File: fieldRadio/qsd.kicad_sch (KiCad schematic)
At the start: 41 parts, among them IC1 MCP1801, IC2 SN74LVC1G04DBVT, IC3 SN74AUP2G79DCUR, IC4 TS5A23157, IC5 SN74CBTLV3253, Q1 J309, T1 T50-TRIFILAR, U1 OPA1678

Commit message: Updating field radio
Continued schematic work on field radio
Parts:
- removed C18, C21: 1nF, Capacitor_SMD:C_0603_1608Metric_Pad1.08x0.95mm_HandSolder, symbol qsd_revB-eagle-import:CAP0603-CAP
- removed R18, R19, R26, R27: 100, Resistor_SMD:R_0603_1608Metric_Pad0.98x0.95mm_HandSolder, symbol qsd_revB-eagle-import:RESISTOR0603-RES
- removed R28: 7.5k, Resistor_SMD:R_0603_1608Metric_Pad0.98x0.95mm_HandSolder, symbol qsd_revB-eagle-import:RESISTOR0603-RES
- removed R31: 10k, Resistor_SMD:R_0603_1608Metric_Pad0.98x0.95mm_HandSolder, symbol qsd_revB-eagle-import:RESISTOR0603-RES
- removed R32: 5K, qsd_revB:RTRIM3296W, symbol qsd_revB-eagle-import:R-TRIMM3296W
- removed R9: R-TRIMM3296W, qsd_revB:RTRIM3296W, symbol qsd_revB-eagle-import:R-TRIMM3296W
- removed U1: OPA1678, Package_SO:SOIC-8_3.9x4.9mm_P1.27mm, symbol Amplifier_Operational:OPA1678
- added C8, C9: 0.1uF, Capacitor_SMD:C_0603_1608Metric_Pad1.08x0.95mm_HandSolder, symbol qsd_revB-eagle-import:CAP0603-CAP
- added IC6, IC7: INA821ID, SOIC127P600X175-8N, symbol SamacSys_Parts:INA821ID
- added R11, R12, R13, R4: 47k, Resistor_SMD:R_0603_1608Metric_Pad0.98x0.95mm_HandSolder, symbol qsd_revB-eagle-import:RESISTOR0603-RES
- added R2, R3: 49.9, Resistor_SMD:R_0603_1608Metric_Pad0.98x0.95mm_HandSolder, symbol qsd_revB-eagle-import:RESISTOR0603-RES
- added R9: 4.32K, Resistor_SMD:R_0603_1608Metric_Pad0.98x0.95mm_HandSolder, symbol qsd_revB-eagle-import:RESISTOR0603-RES
- C12, C14: value 0.22uF -> 0.1uF
- C13, C15: value 0.22uF -> 470pF
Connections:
- net 0-DEG: now also C13.2, IC6.4 (+IN), R4.2; no longer C12.2
- net 180-DEG: now also C13.1, IC6.1 (-IN), R11.2; no longer C13.2
- net 270-DEG: now also IC7.1 (-IN), R12.2
- net 90-DEG: now also C15.1, IC7.4 (+IN), R13.2; no longer C14.2
- net GND: now also C12.2, C8.1, C9.1, IC6.5 (-VS), IC7.5 (-VS), R11.1, R12.1, R13.1, R4.1, R9.1; no longer C12.1, C13.1, C15.1
- net Iout: now also IC6.7 (OUT)
- net Qout: now also IC7.7 (OUT)
- net at C6.2, C7.1 (+), R8.1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: now also R9.2
- net VCC5 renamed VDD5
- net VDD5: now also C8.2, C9.2, IC6.8 (+VS), IC7.8 (+VS)
- new net: IC7.2 (RG_1), R2.1
- new net: IC7.3 (RG_2), R2.2
- new net: IC6.2 (RG_1), R3.1
- new net: IC6.3 (RG_2), R3.2
- new net vbias: C12.1, C14.2, IC6.6 (REF), IC7.6 (REF)
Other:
- note added: "VBIAS"

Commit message: More schematic dev.
More schematic development
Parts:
- renumbered C1 to C128, C2 to C129, C3 to C130, C4 to C131, C16 to C132, C5 to C133, C6 to C134, C7 to C135, C10 to C136, C11 to C137, C13 to C138, C15 to C139, C8 to C140, C9 to C141, C12 to C142, C14 to C143, C19 to C144, C20 to C145, JP7 to JP3, Q1 to Q24, R1 to R143, R5 to R144, R6 to R145, R7 to R146, R8 to R147, R9 to R148, R10 to R149, R4 to R150, R11 to R151, R12 to R152, R13 to R153, R2 to R154, R3 to R155, T1 to T2

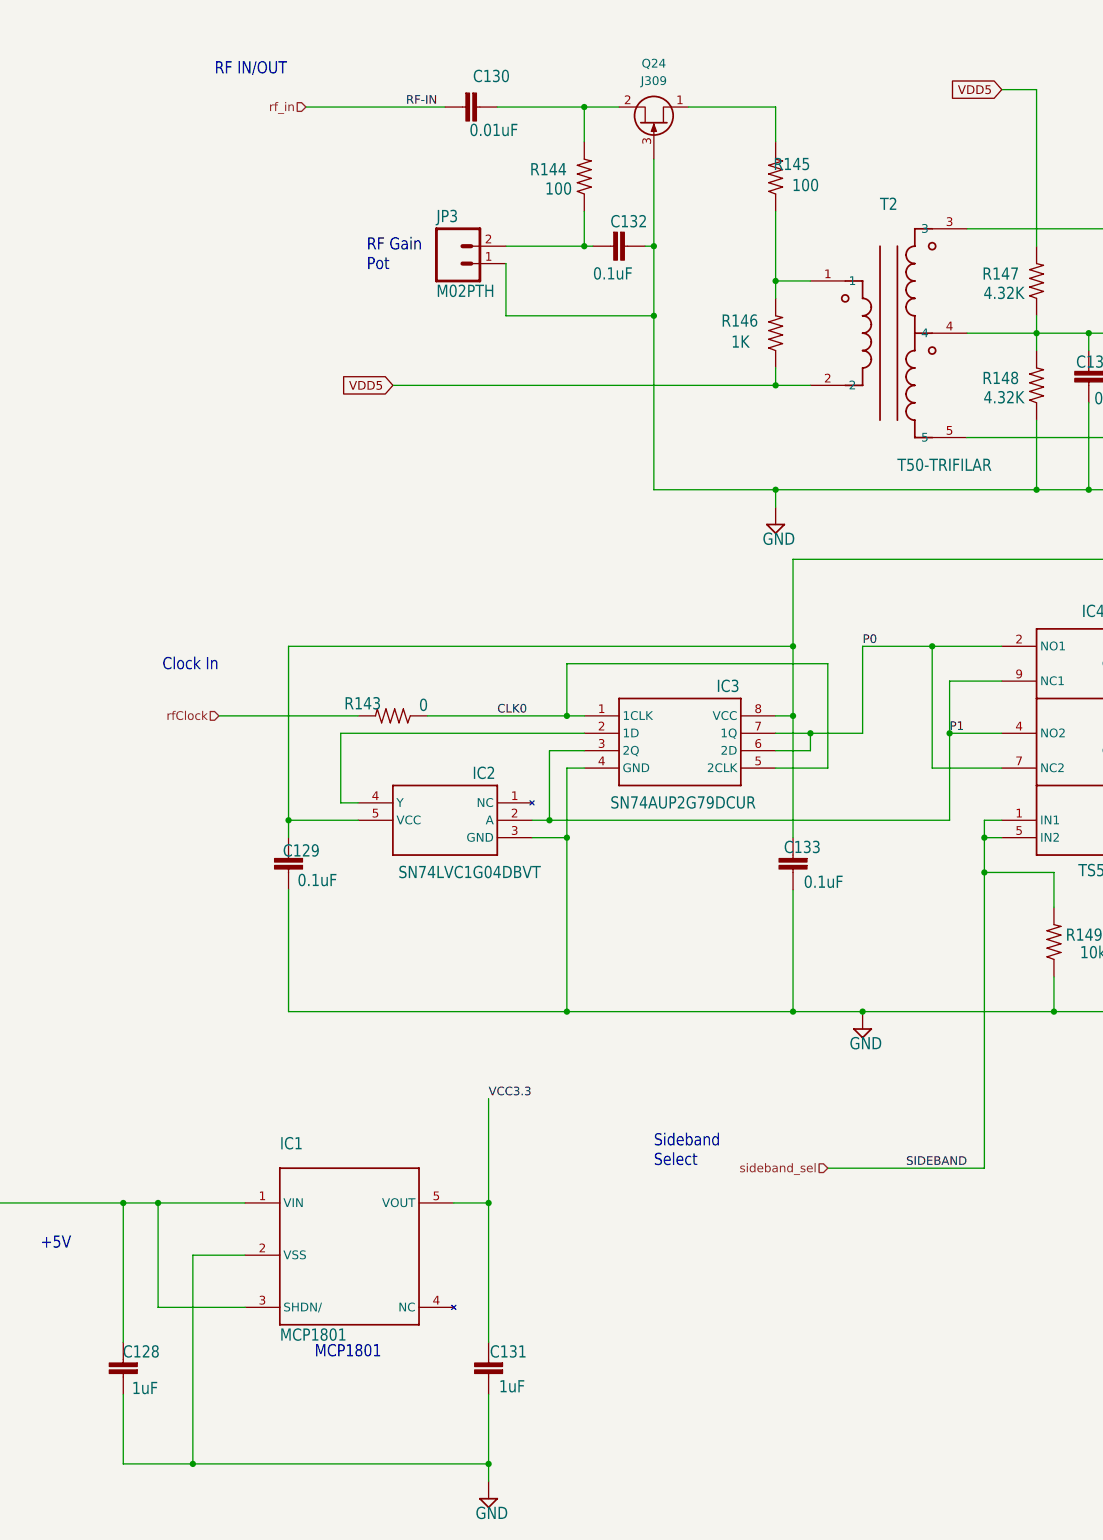
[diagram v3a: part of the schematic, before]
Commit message: Update Connectors
Changed to PCB mount connectors for back panel
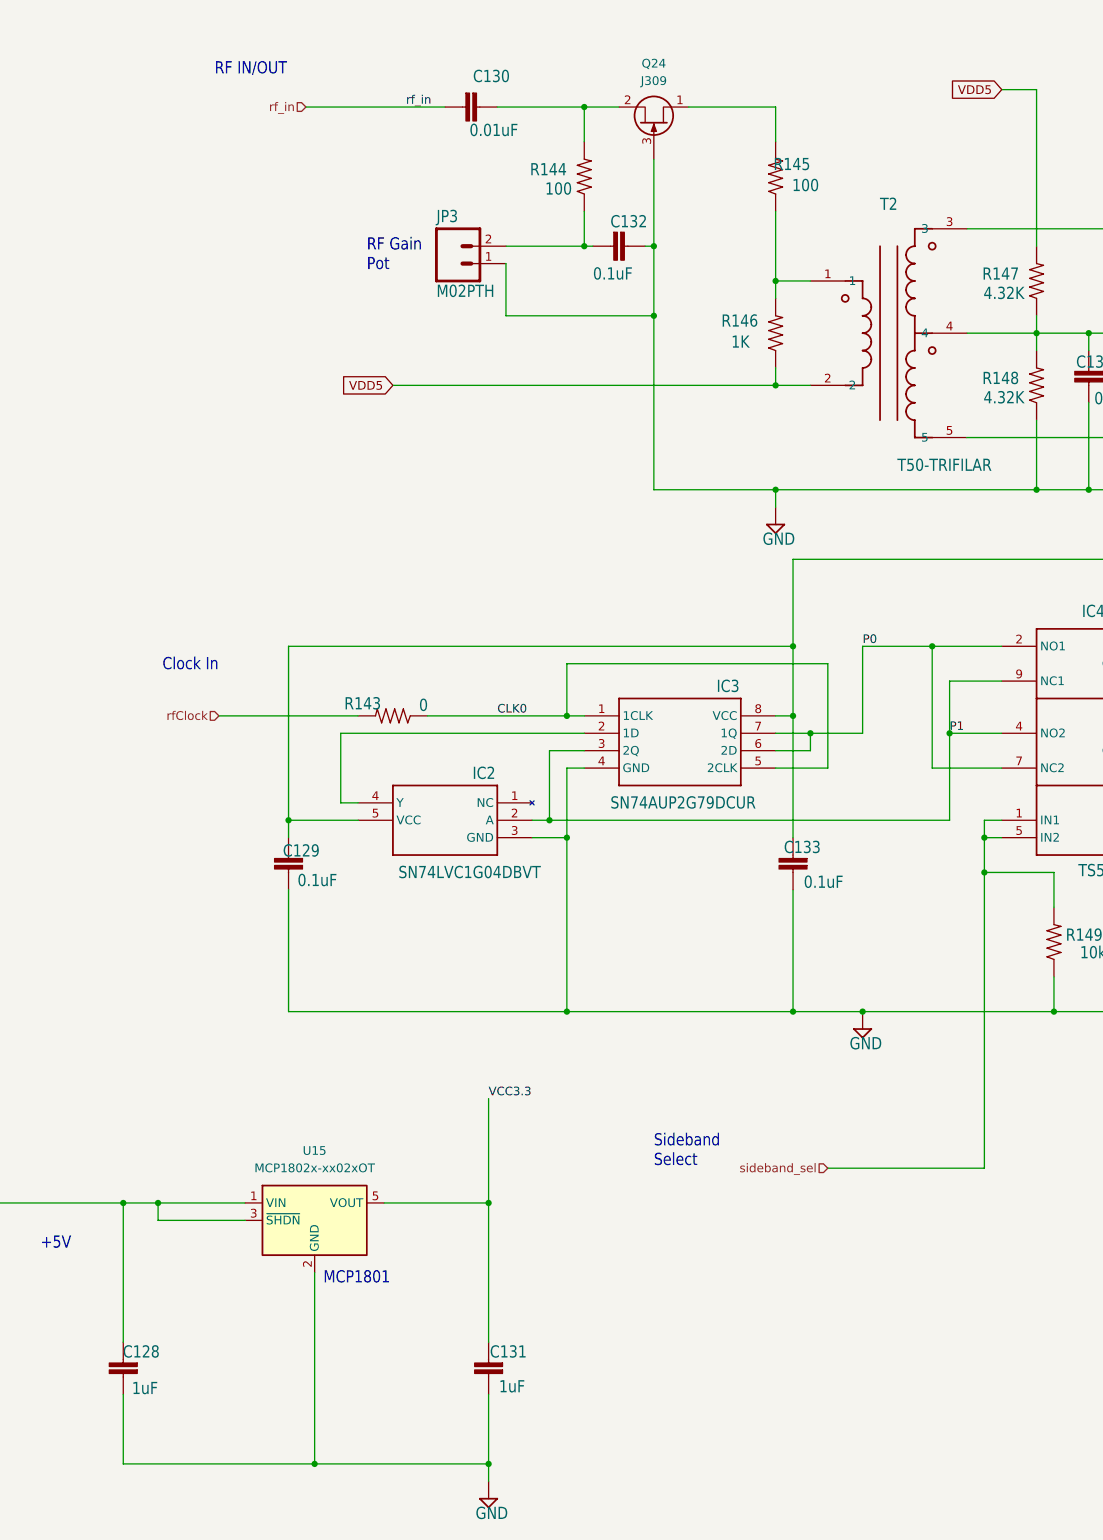
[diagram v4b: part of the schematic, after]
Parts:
- removed IC1: MCP1801, qsd_revB:SOT23-5, symbol qsd_revB-eagle-import:MCP1801
- added U15: MCP1802x-xx02xOT, Package_TO_SOT_SMD:SOT-23-5, symbol Regulator_Linear:MCP1802x-xx02xOT
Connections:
- net GND: now also U15.2 (GND)
- net VCC3.3: now also U15.5 (VOUT)
- net VDD5: now also U15.1 (VIN), U15.3 (~{SHDN})
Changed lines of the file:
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@@
   (junction (at 269.24 96.52) (diameter 0) (color 0 0 0 0)
   )
-  (junction (at 62.23 246.38) (diameter 0) (color 0 0 0 0)
-  )
   (junction (at 177.8 160.02) (diameter 0) (color 0 0 0 0)
   )
@@
   (junction (at 264.16 127) (diameter 0) (color 0 0 0 0)
   )
+  (junction (at 80.01 246.38) (diameter 0) (color 0 0 0 0)
+  )
   (junction (at 57.15 208.28) (diameter 0) (color 0 0 0 0)
   )
@@
     (stroke (width 0) (type default))
   )
-  (wire (pts (xy 52.07 246.38) (xy 62.23 246.38))
+  (wire (pts (xy 52.07 246.38) (xy 80.01 246.38))
     (stroke (width 0) (type default))
   )
@@
     (stroke (width 0) (type default))
   )
+  (wire (pts (xy 80.01 218.44) (xy 80.01 246.38))
+    (stroke (width 0) (type default))
+  )
   (wire (pts (xy 381 107.95) (xy 381 105.41))
     (stroke (width 0) (type default))
@@
     (stroke (width 0) (type default))
   )
+  (wire (pts (xy 80.01 246.38) (xy 105.41 246.38))
+    (stroke (width 0) (type default))
+  )
   (wire (pts (xy 392.43 73.66) (xy 392.43 82.55))
     (stroke (width 0) (type default))
@@
     (stroke (width 0) (type default))
   )
-  (wire (pts (xy 69.85 215.9) (xy 62.23 215.9))
-    (stroke (width 0) (type default))
-  )
   (wire (pts (xy 154.94 129.54) (xy 116.84 129.54))
     (stroke (width 0) (type default))
@@
     (stroke (width 0) (type default))
   )
-  (wire (pts (xy 100.33 208.28) (xy 105.41 208.28))
+  (wire (pts (xy 90.17 208.28) (xy 105.41 208.28))
     (stroke (width 0) (type default))
   )
@@
     (stroke (width 0) (type default))
   )
-  (wire (pts (xy 69.85 223.52) (xy 57.15 223.52))
+  (wire (pts (xy 69.85 210.82) (xy 57.15 210.82))
     (stroke (width 0) (type default))
   )
@@
     (stroke (width 0) (type default))
   )
-  (wire (pts (xy 62.23 246.38) (xy 105.41 246.38))
-    (stroke (width 0) (type default))
-  )
   (wire (pts (xy 152.4 139.7) (xy 152.4 142.24))
     (stroke (width 0) (type default))
@@
     (stroke (width 0) (type default))
   )
-  (wire (pts (xy 62.23 215.9) (xy 62.23 246.38))
-    (stroke (width 0) (type default))
-  )
   (wire (pts (xy 107.95 78.74) (xy 129.54 78.74))
     (stroke (width 0) (type default))
@@
     (stroke (width 0) (type default))
   )
-  (wire (pts (xy 57.15 223.52) (xy 57.15 208.28))
+  (wire (pts (xy 57.15 210.82) (xy 57.15 208.28))
     (stroke (width 0) (type default))
   )
@@
     (effects (font (size 1.778 1.5113)) (justify left bottom))
   )
-  (text "MCP1801" (at 80.01 231.14 0)
+  (text "MCP1801" (at 81.28 220.345 0)
     (effects (font (size 1.778 1.5113)) (justify left bottom))
   )
@@
     (effects (font (size 2.54 2.159)) (justify left bottom))
   )
-  (label "RF-IN" (at 93.345 48.26 0) (fields_autoplaced)
+  (label "rf_in" (at 93.345 48.26 0) (fields_autoplaced)
     (effects (font (size 1.2446 1.2446)) (justify left bottom))
   )
@@
   )
   (label "VCC3.3" (at 105.41 193.04 0) (fields_autoplaced)
-    (effects (font (size 1.2446 1.2446)) (justify left bottom))
-  )
-  (label "SIDEBAND" (at 166.37 203.2 0) (fields_autoplaced)
     (effects (font (size 1.2446 1.2446)) (justify left bottom))
   )
@@
   (hierarchical_label "Qout" (shape output) (at 394.97 87.63 0) (fields_autoplaced)
     (effects (font (size 1.27 1.27)) (justify left))
+  )
+  (symbol (lib_id "Regulator_Linear:MCP1802x-xx02xOT") (at 80.01 210.82 0) (unit 1)
+    (in_bom yes) (on_board yes) (dnp no) (fields_autoplaced)
+    (property "Reference" "U15" (at 80.01 200.66 0)
+      (effects (font (size 1.27 1.27)))
+    )
+    (property "Value" "MCP1802x-xx02xOT" (at 80.01 203.2 0)
+      (effects (font (size 1.27 1.27)))
+    )
+    (property "Footprint" "Package_TO_SOT_SMD:SOT-23-5" (at 73.66 201.93 0)
+      (effects (font (size 1.27 1.27) italic) (justify left) hide)
+    )
+    (property "Datasheet" "http://ww1.microchip.com/downloads/en/DeviceDoc/22053C.pdf" (at 80.01 213.36 0)
+      (effects (font (size 1.27 1.27)) hide)
+    )
+    (pin "5")
+    (pin "1")
+    (pin "4")
+    (pin "3")
+    (pin "2")
+    (instances
+      (project "fieldRadio"
+        (path "/a1d1b2b0-2f27-4dc0-94ba-bb0e02933617/b9a43a44-ac26-41be-aaf6-05c85180cb06"
+          (reference "U15") (unit 1)
+        )
+      )
+    )
   )
   (symbol (lib_id "Device:Q_NJFET_DSG") (at 129.54 50.8 270) (mirror x) (unit 1)
@@
         )
       )
-    )
-  )
-  (symbol (lib_id "qsd_revB-eagle-import:MCP1801") (at 74.93 226.06 0) (unit 1)
-    (in_bom yes) (on_board yes) (dnp no)
-    (property "Reference" "IC1" (at 74.93 200.66 0)
-      (effects (font (size 1.778 1.5113)) (justify left bottom))
-    )
-    (property "Value" "MCP1801" (at 74.93 228.6 0)
-      (effects (font (size 1.778 1.5113)) (justify left bottom))
-    )
-    (property "Footprint" "qsd_revB:SOT23-5" (at 74.93 226.06 0)
-      (effects (font (size 1.27 1.27)) hide)
-    )
-    (property "Datasheet" "" (at 74.93 226.06 0)
-      (effects (font (size 1.27 1.27)) hide)
-    )
-    (pin "1")
-    (pin "2")
-    (pin "3")
-    (pin "4")
-    (pin "5")
-    (instances
-      (project "fieldRadio"
-        (path "/a1d1b2b0-2f27-4dc0-94ba-bb0e02933617/b9a43a44-ac26-41be-aaf6-05c85180cb06"
-          (reference "IC1") (unit 1)
-        )
-      )
-      (project "qsd_revC"
-        (path "/f12afe60-319a-4dbd-9291-4cc8914dd5dd"
-          (reference "IC1") (unit 1)
-        )
-      )

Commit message: Clean Up
Schematic clean up in prep for layout
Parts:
- renumbered C128 to C135, C129 to C136, C130 to C137, C131 to C138, C132 to C139, C133 to C140, C134 to C141, C135 to C142, C136 to C143, C137 to C144, C138 to C145, C139 to C146, C140 to C147, C141 to C148, C142 to C149, C143 to C150, C144 to C151, C145 to C152, IC2 to IC3, IC3 to IC4, IC4 to IC5, IC5 to IC6, IC6 to IC7, IC7 to IC8, JP3 to JP2, Q24 to Q20, R143 to R136, R144 to R137, R145 to R138, R146 to R139, R147 to R140, R148 to R141, R149 to R142, R150 to R143, R151 to R144, R152 to R145, R153 to R146, R154 to R147, R155 to R148, U15 to U9
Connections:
- net sideband_sel renamed SIDEBAND_SEL

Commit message: Placement Update
LPF and TR Switch placed
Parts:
- C142, C151: footprint qsd_revB:CPOL-RADIAL-10UF-25V -> Capacitor_THT:CP_Radial_D6.3mm_P2.50mm
- IC3: footprint qsd_revB:SOT95P280X145-5N -> Package_TO_SOT_SMD:SOT-23-5_HandSoldering
- IC4: footprint qsd_revB:SOP50P310X90-8N -> Package_SO:VSSOP-8_2.3x2mm_P0.5mm
- IC5: footprint qsd_revB:MSOP10 -> Package_SO:VSSOP-10_3x3mm_P0.5mm
- IC6: footprint qsd_revB:TSSOP16 -> Package_SO:TSSOP-16_4.4x5mm_P0.65mm
- IC7, IC8: footprint SOIC127P600X175-8N -> SamacSys_Parts:SOIC127P600X175-8N
- JP2: footprint qsd_revB:1X02 -> Connector_PinHeader_2.54mm:PinHeader_1x02_P2.54mm_Vertical
- T2: footprint qsd_revB:T50-TRIFILAR -> qsd:T50-TRIFILAR
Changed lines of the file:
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@@
       (effects (font (size 1.778 1.5113)) (justify left bottom))
     )
-    (property "Footprint" "qsd_revB:MSOP10" (at 185.42 157.48 0)
+    (property "Footprint" "Package_SO:VSSOP-10_3x3mm_P0.5mm" (at 185.42 157.48 0)
       (effects (font (size 1.27 1.27)) hide)
     )
@@
       (effects (font (size 1.778 1.5113)) (justify left bottom))
     )
-    (property "Footprint" "qsd_revB:TSSOP16" (at 236.22 119.38 0)
+    (property "Footprint" "Package_SO:TSSOP-16_4.4x5mm_P0.65mm" (at 236.22 119.38 0)
       (effects (font (size 1.27 1.27)) hide)
     )
@@
       (effects (font (size 1.778 1.5113)) (justify left bottom))
     )
-    (property "Footprint" "qsd_revB:CPOL-RADIAL-10UF-25V" (at 200.66 86.36 0)
+    (property "Footprint" "Capacitor_THT:CP_Radial_D6.3mm_P2.50mm" (at 200.66 86.36 0)
       (effects (font (size 1.27 1.27)) hide)
     )
@@
       (effects (font (size 1.27 1.27)))
     )
-    (property "Footprint" "SOIC127P600X175-8N" (at 365.76 68.58 0)
+    (property "Footprint" "SamacSys_Parts:SOIC127P600X175-8N" (at 365.76 68.58 0)
       (effects (font (size 1.27 1.27)) (justify left) hide)
     )
@@
       (effects (font (size 1.778 1.5113)) (justify left bottom))
     )
-    (property "Footprint" "qsd_revB:1X02" (at 100.33 71.12 0)
+    (property "Footprint" "Connector_PinHeader_2.54mm:PinHeader_1x02_P2.54mm_Vertical" (at 100.33 71.12 0)
       (effects (font (size 1.27 1.27)) hide)
     )
@@
       (effects (font (size 1.778 1.5113)) (justify left))
     )
-    (property "Footprint" "qsd_revB:SOT95P280X145-5N" (at 111.76 149.86 0)
+    (property "Footprint" "Package_TO_SOT_SMD:SOT-23-5_HandSoldering" (at 111.76 149.86 0)
       (effects (font (size 1.27 1.27)) hide)
     )
@@
       (effects (font (size 1.778 1.5113)) (justify left))
     )
-    (property "Footprint" "qsd_revB:SOP50P310X90-8N" (at 124.46 133.35 0)
+    (property "Footprint" "Package_SO:VSSOP-8_2.3x2mm_P0.5mm" (at 124.46 133.35 0)
       (effects (font (size 1.27 1.27)) hide)
     )
@@
       (effects (font (size 1.778 1.5113)) (justify left bottom))
     )
-    (property "Footprint" "qsd_revB:CPOL-RADIAL-10UF-25V" (at 388.62 38.1 0)
+    (property "Footprint" "Capacitor_THT:CP_Radial_D6.3mm_P2.50mm" (at 388.62 38.1 0)
       (effects (font (size 1.27 1.27)) hide)
     )
@@
       (effects (font (size 1.778 1.5113)) (justify left bottom))
     )
-    (property "Footprint" "qsd_revB:T50-TRIFILAR" (at 157.48 88.9 0)
+    (property "Footprint" "qsd:T50-TRIFILAR" (at 157.48 88.9 0)
       (effects (font (size 1.27 1.27)) hide)
     )
@@
       (effects (font (size 1.27 1.27)))
     )
-    (property "Footprint" "SOIC127P600X175-8N" (at 365.76 97.79 0)
+    (property "Footprint" "SamacSys_Parts:SOIC127P600X175-8N" (at 365.76 97.79 0)
       (effects (font (size 1.27 1.27)) (justify left) hide)
     )

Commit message: Placement Refinement 1
Ungrouping blocks and optimizing placement
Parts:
- C145, C146: value 470pF -> 330pF
- R147, R148: value 49.9 -> 499
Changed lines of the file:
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@@
       (effects (font (size 1.778 1.5113)) (justify left bottom))
     )
-    (property "Value" "470pF" (at 293.37 104.14 0)
+    (property "Value" "330pF" (at 293.37 104.14 0)
       (effects (font (size 1.778 1.5113)) (justify left bottom))
     )
@@
       (effects (font (size 1.27 1.27)) hide)
     )
+    (property "Mouser Part Number" "" (at 284.48 101.6 0)
+      (effects (font (size 1.27 1.27)) hide)
+    )
     (pin "1")
     (pin "2")
@@
       (effects (font (size 1.778 1.5113)) (justify left bottom))
     )
-    (property "Value" "470pF" (at 292.1 88.9 0)
+    (property "Value" "330pF" (at 292.1 88.9 0)
       (effects (font (size 1.778 1.5113)) (justify left bottom))
     )
@@
       (effects (font (size 1.27 1.27)) hide)
     )
+    (property "Mouser Part Number" "" (at 284.48 85.09 0)
+      (effects (font (size 1.27 1.27)) hide)
+    )
     (pin "1")
     (pin "2")
@@
       (effects (font (size 1.778 1.5113)) (justify left bottom))
     )
-    (property "Value" "49.9" (at 337.82 100.33 0)
+    (property "Value" "499" (at 337.82 100.33 0)
       (effects (font (size 1.778 1.5113)) (justify left bottom))
     )
@@
     )
     (property "Datasheet" "" (at 330.2 102.87 0)
+      (effects (font (size 1.27 1.27)) hide)
+    )
+    (property "Mouser Part Number" "" (at 330.2 102.87 0)
       (effects (font (size 1.27 1.27)) hide)
     )
@@
   (symbol (lib_id "qsd_revB-eagle-import:RESISTOR0603-RES") (at 147.32 58.42 90) (unit 1)
     (in_bom yes) (on_board yes) (dnp no)
-    (property "Reference" "R138" (at 152.4 55.6006 90)
+    (property "Reference" "R138" (at 154.305 55.88 90)
       (effects (font (size 1.778 1.5113)) (justify left bottom))
     )
@@
       (effects (font (size 1.778 1.5113)) (justify left bottom))
     )
-    (property "Value" "49.9" (at 341.63 71.12 0)
+    (property "Value" "499" (at 341.63 71.12 0)
       (effects (font (size 1.778 1.5113)) (justify left bottom))
     )
@@
       (effects (font (size 1.27 1.27)) hide)
     )
+    (property "Mouser Part Number" "" (at 334.01 73.66 0)
+      (effects (font (size 1.27 1.27)) hide)
+    )
